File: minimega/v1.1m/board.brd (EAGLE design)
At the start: 50 x 42 mm, 16 parts, among them U1 ATMEGA328P_PDIP, Y1 16MHz

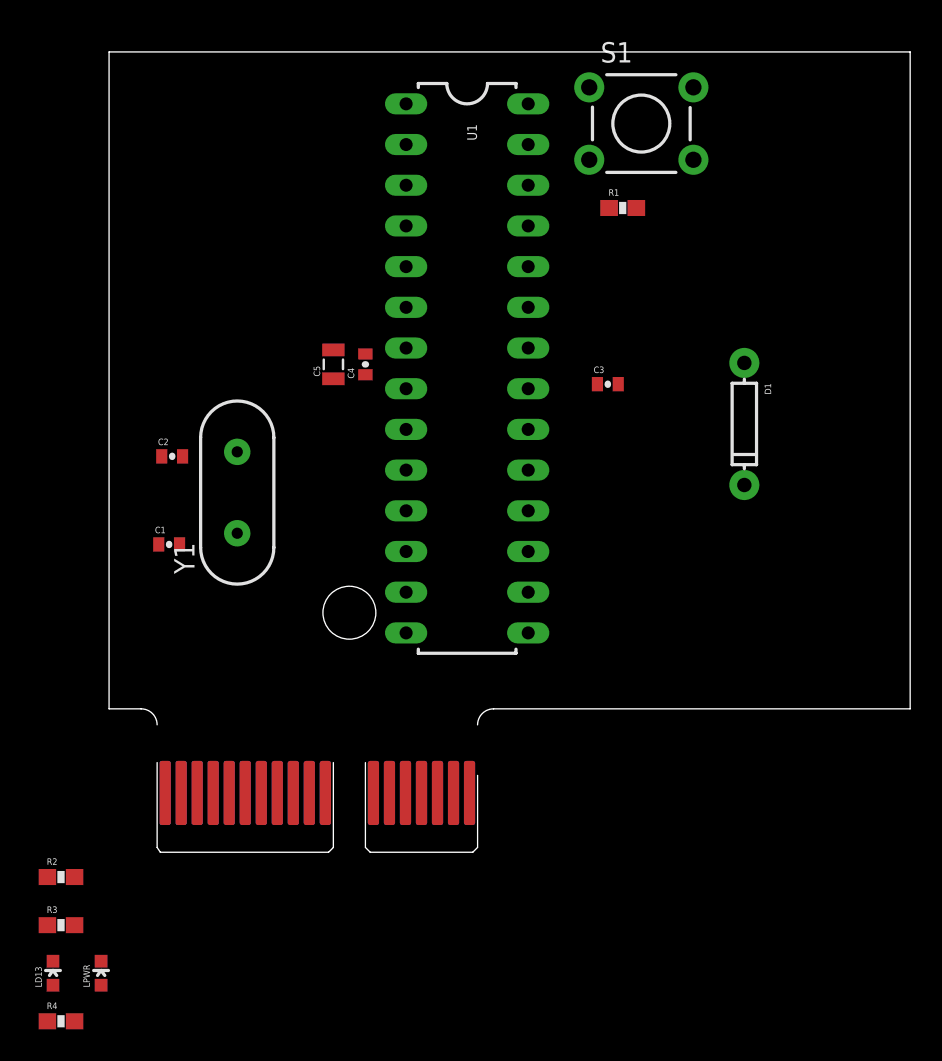
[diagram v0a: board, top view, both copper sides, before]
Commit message: rerouted parts of the modboard backplane to put the {2,3}{D,E} lanes on the NC lines
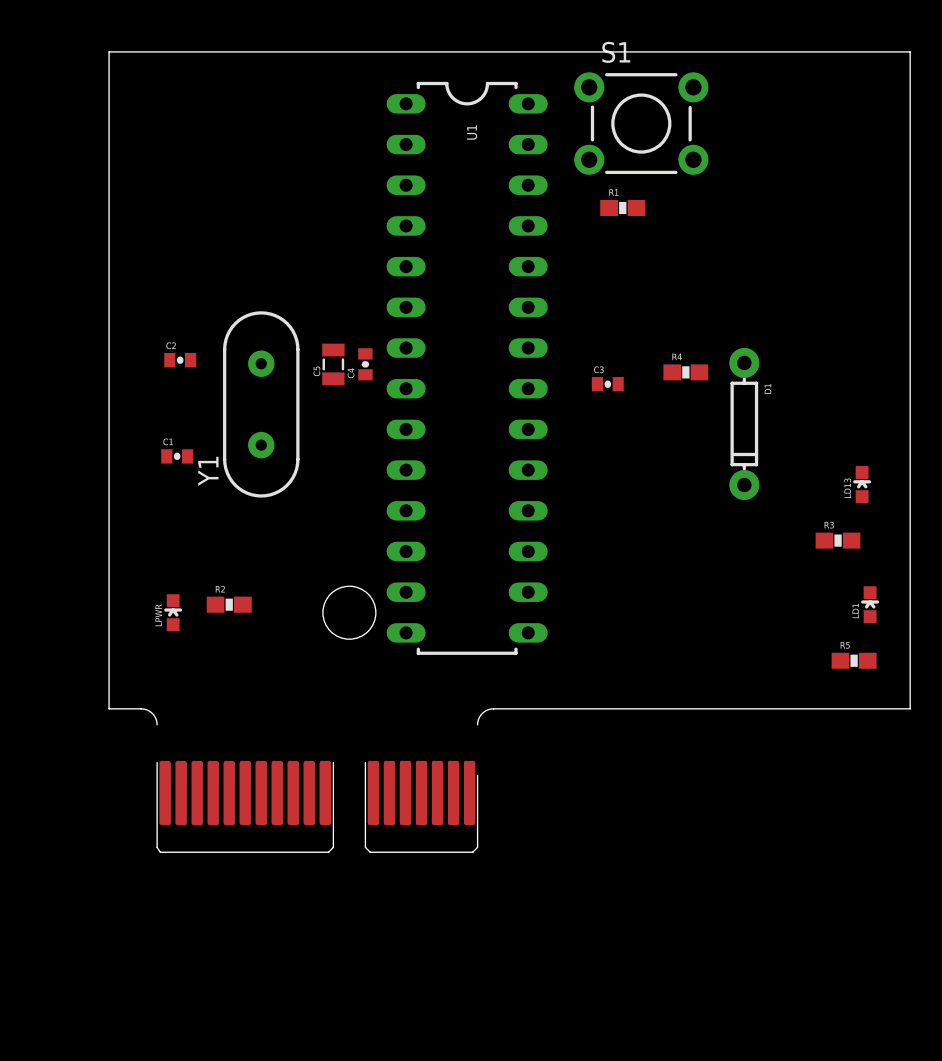
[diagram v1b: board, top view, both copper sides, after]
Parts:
- added LD1: GRN, SparkFun-LED:LED-0603
- added R5: 220, SparkFun-Resistors:0603-RES
- moved LD13 59.0 mm to (47.0, 23.0)
- moved R4 56.2 mm to (36.0, 30.0)
- moved R3 54.1 mm to (45.5, 19.5)
- moved LPWR 22.9 mm to (4.00, 15.0)
- moved R2 20.0 mm to (7.50, 15.5)
- moved C2 6.02 mm to (4.44, 30.8)
- moved Y1 5.70 mm to (9.50, 28.0)
- moved C1 5.52 mm to (4.25, 24.8)
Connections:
- new net E0: U$1.A14, U1.12
- new net E3: U$1.B9, U1.13
- new net N$7: LD1.A, R5.1
- net C2: now also R5.2; no longer U1.12
- net GND: now also LD1.C; no longer U$1.A14, U$1.B9
